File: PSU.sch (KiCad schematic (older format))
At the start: 47 parts, among them U10 SGM3204, U11 MP2359, U12 XC6206P332MR, U13 MC34063ABD-TR, U14 TX4314, U15 MAX889RESA+

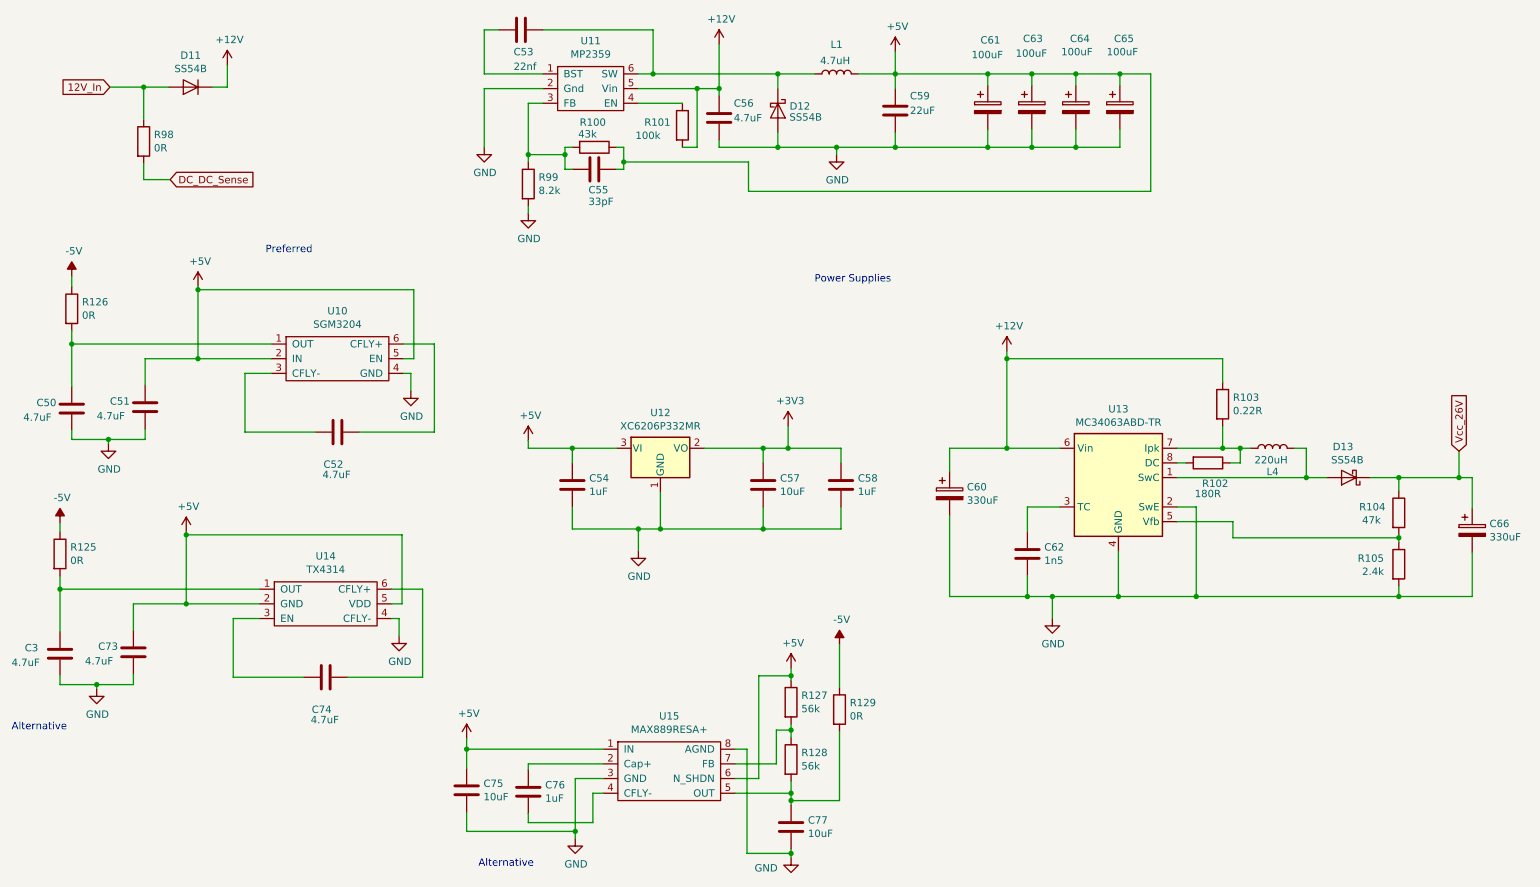
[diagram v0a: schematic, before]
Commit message: removed SG3204 and TX4313 -5V charge pumps and added LM2776 in their place
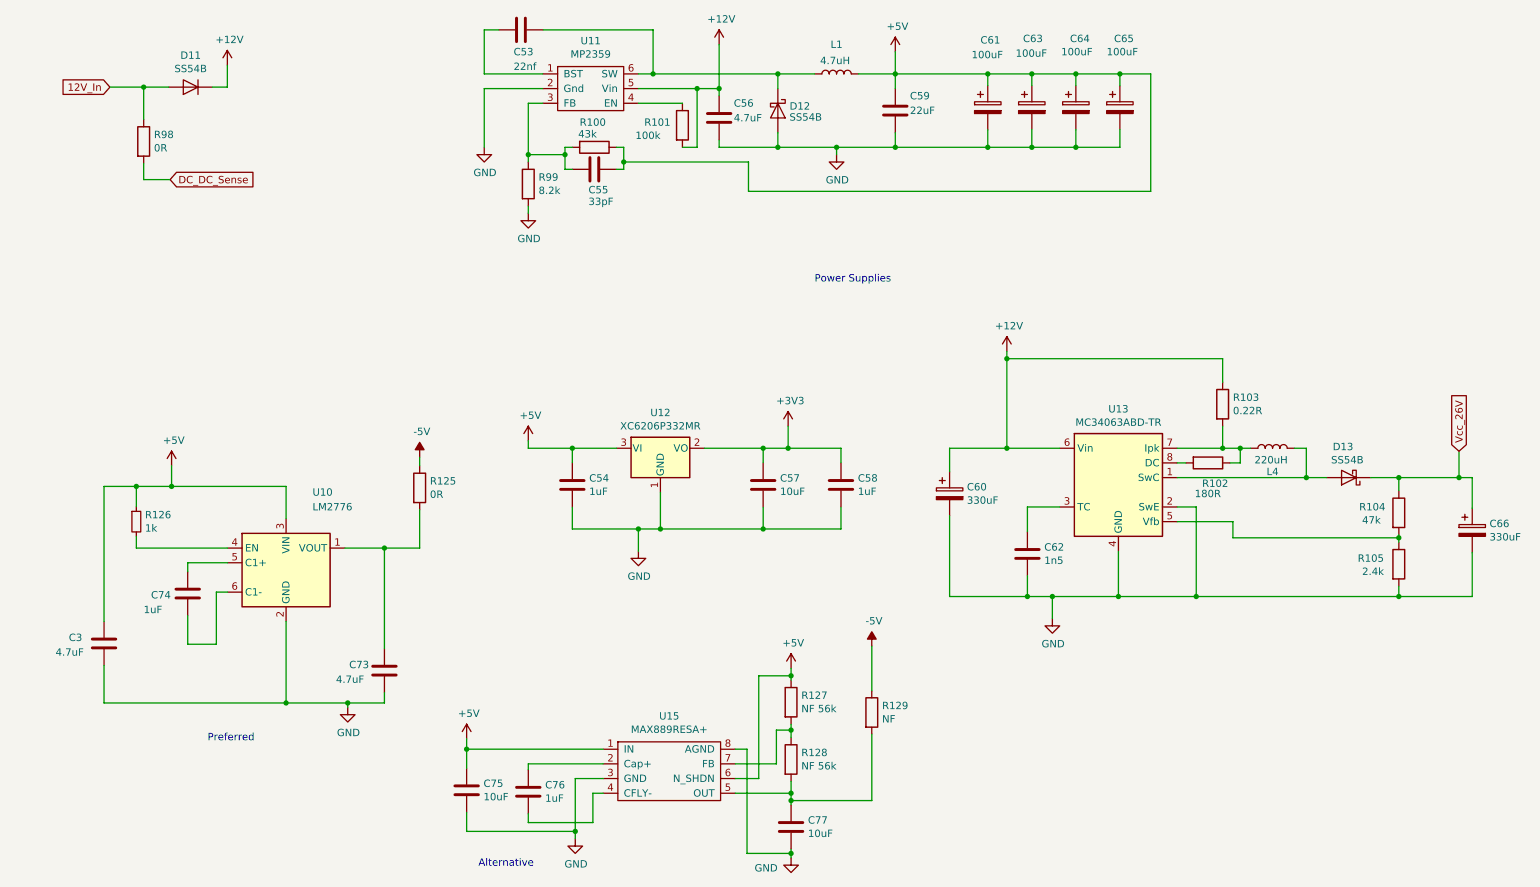
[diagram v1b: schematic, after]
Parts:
- removed C50, C51, C52: 4.7uF, Capacitor_SMD:C_0805_2012Metric, symbol Device:C
- removed R126: 0R, Resistor_SMD:R_0603_1608Metric, symbol Device:R
- removed U10: SGM3204, Package_TO_SOT_SMD:SOT-23-6, symbol Regulators_Custom:SGM3204
- removed U14: TX4314, Package_TO_SOT_SMD:SOT-23-6, symbol Regulators_Custom:TX4314
- added R126: 1k, Resistor_SMD:R_0603_1608Metric, symbol Device:R_Small
- added U10: LM2776, Package_TO_SOT_SMD:SOT-23-6, symbol Regulator_SwitchedCapacitor:LM2776
- C74: value 4.7uF -> 1uF; JLPCB Component C1779 -> C15849
- R127, R128: value 56k -> NF 56k
- R129: value 0R -> NF
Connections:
- net +5V: now also C3.1, R126.1, U10.3 (VIN); no longer C73.1
- net GND: now also U10.2 (GND)
- net at R125.2: now also C73.1, U10.1 (VOUT); no longer C3.1
- net at C74.1: now also U10.5 (C1+)
- net at C74.2: now also U10.6 (C1-)
- new net: R126.2, U10.4 (EN)
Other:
- moved on the sheet: C3, C73, C74, R125, R129
